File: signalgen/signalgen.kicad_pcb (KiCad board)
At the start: 2 copper layers, 54 parts, among them CON1 USB-MINI-B, J1 SWDCONN, P1 BNC, U1 OSC-16MHZ, U10 ADA4805-1, U2 ADP1715-3.3, U3 STM32F030F4, U4 CP2102, U5 OSC-50MHZ, U6 LTC1983-5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

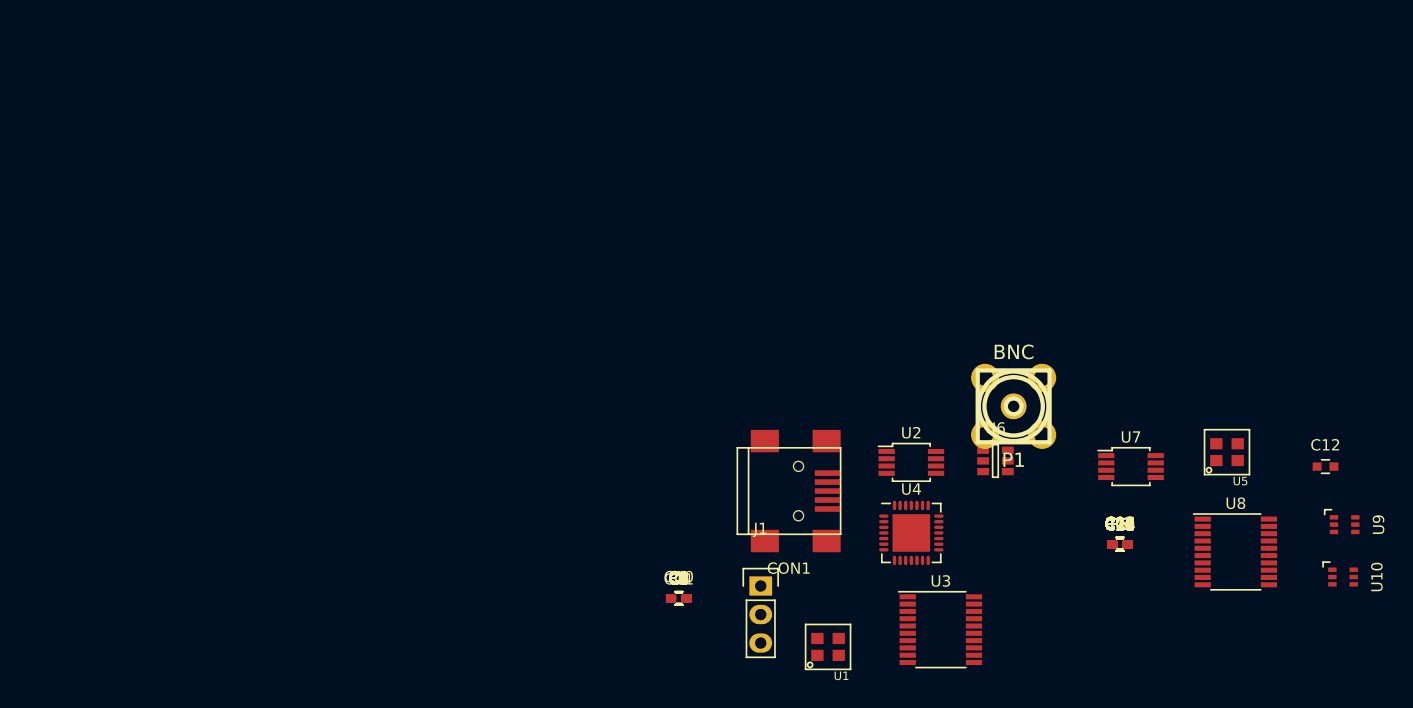
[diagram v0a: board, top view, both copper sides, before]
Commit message: First layout of DDS signal generator.
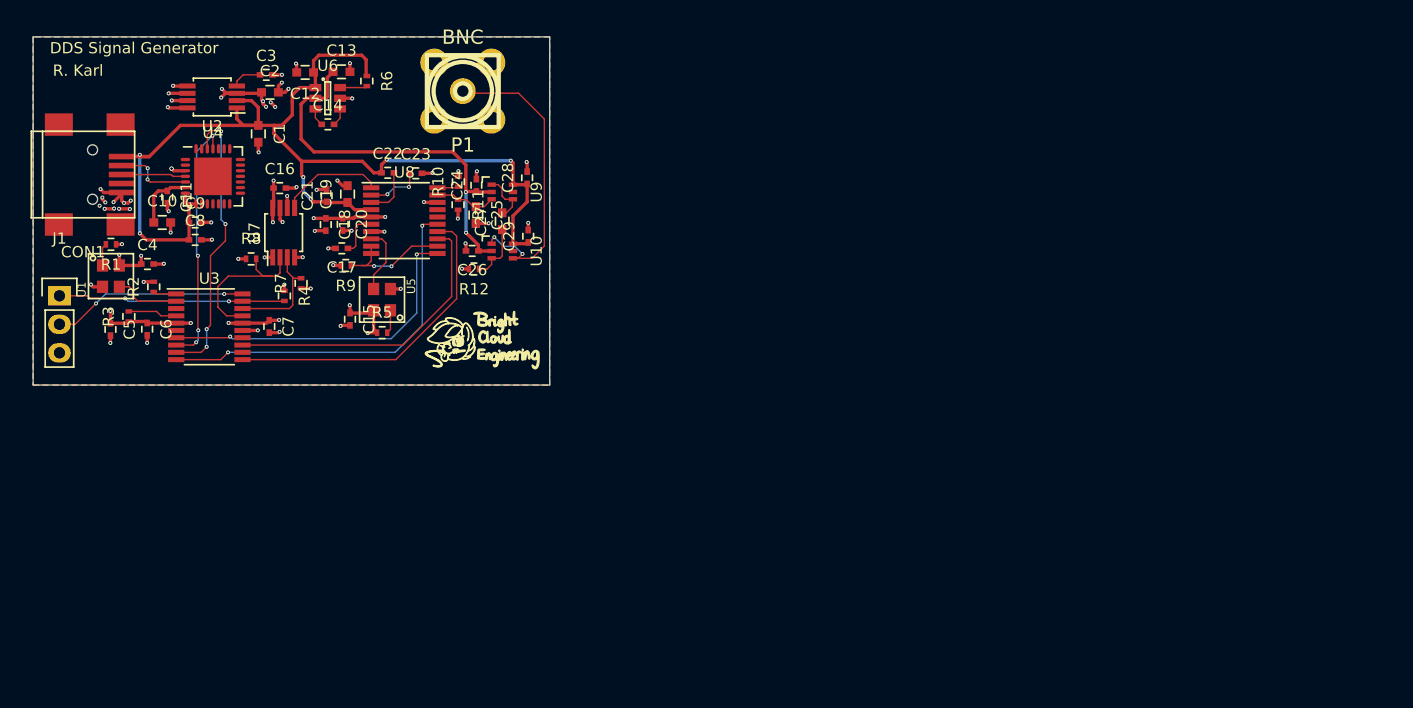
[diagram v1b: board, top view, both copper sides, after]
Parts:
- added G***: LOGO, kicad:LOGOFRONT, F.Cu at (131.0, 82.0)
- moved C12 97.4 mm to (115.2, 58.2), turned to 180 degrees
- moved R8 81.4 mm to (110.4, 74.8)
- moved C16 81.3 mm to (113.0, 68.5)
- moved C13 81.1 mm to (118.5, 58.1)
- moved U9 80.6 mm to (132.8, 68.8)
- moved U10 80.3 mm to (132.8, 74.1)
- moved C14 79.8 mm to (117.2, 62.8)
- moved U8 79.7 mm to (124.1, 71.4)
- moved R6 78.7 mm to (120.7, 58.9), turned to 270 degrees
- moved U7 78.3 mm to (113.3, 72.4), turned to 90 degrees
- moved C21 77.2 mm to (117.1, 69.1), turned to 90 degrees
- moved R7 76.5 mm to (114.9, 76.9), turned to 90 degrees
- moved U5 76.5 mm to (122.1, 78.4), turned to 90 degrees
- moved C18 76.2 mm to (117.1, 71.7), turned to 270 degrees
- moved C19 75.5 mm to (119.0, 69.0), turned to 90 degrees
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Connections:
- C29 pad 2: Net-(C29-Pad2) -> GND
- U8 pad 20: Net-(U8-Pad20) -> Net-(R10-Pad1)
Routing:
- net +5V: track 0.00 -> 99.0 mm, vias 0 -> 6
- net GND: track 0.00 -> 55.6 mm, vias 0 -> 59
- net +3V3: track 0.00 -> 43.5 mm, vias 0 -> 22
- net -5V: track 0.00 -> 35.5 mm, vias 0 -> 2
- net DDSNSS: track 0.00 -> 33.4 mm, vias 0 -> 2
- net DDSRESET: track 0.00 -> 29.6 mm, vias 0 -> 2
- net DDSSCK: track 0.00 -> 28.8 mm
- net VOUT: track 0.00 -> 27.7 mm, vias 0 -> 2
- net DDSMOSI: track 0.00 -> 26.7 mm
- net /usbbridge/TXD: track 0.00 -> 25.6 mm, vias 0 -> 4
- net /usbbridge/RXD: track 0.00 -> 22.2 mm, vias 0 -> 4
- net MCUSWDIO: track 0.00 -> 20.2 mm, vias 0 -> 2
- net MCUSWCLK: track 0.00 -> 17.4 mm, vias 0 -> 2
- net SCL: track 0.00 -> 14.4 mm
- net Net-(R9-Pad1): track 0.00 -> 10.8 mm, vias 0 -> 2
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- added copper zone on In1.Cu, net +3V3
- added copper zone on F.Cu, net +5V
- added copper zone on B.Cu, net GND
- added copper zone on In2.Cu, net GND
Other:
- board outline added: 46 x 31 mm
- copper layers 2 -> 4
- net class Default: clearance 0.2 -> 0.127; trace_width 0.25 -> 0.127; via_dia 0.6 -> 0.3554; via_drill 0.4 -> 0.254
- net class Power added: clearance 0.127, trace_width 0.3, via_dia 0.3554, via_drill 0.254
- rule trace_clearance: 0.2 -> 0.127
- rule trace_min: 0.2 -> 0.127
- rule via_min_drill: 0.3 -> 0.254
- rule via_min_size: 0.4 -> 0.3554
- board text added: "DDS Signal Generator"
- board text added: "R. Karl"
